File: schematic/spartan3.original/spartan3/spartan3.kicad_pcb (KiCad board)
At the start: 2 copper layers, 215.9 x 160 mm, 241 parts, among them U1_clk_select_0 SPFT_Sliding_Switch-dynacore, U2 XC3S250E-4TQG144C

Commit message: Schematics :: in/out pins mapped. PCB layout :: updated
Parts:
- removed J_CONTROL_0: Conn_01x25_Male, Connector_PinHeader_2.54mm:PinHeader_1x25_P2.54mm_Vertical
- F_pwr_0, U_pwr_vcc_banks_0, U_pwr_vcc_core_0, U_pwr_vcc_peripheral_0: moved to B.Cu
- moved X_clk_0 243.8 mm to (243.9, 44.4)
- moved U_pwr_vcc_banks_0 59.2 mm to (206.3, 50.8)
- moved U_pwr_vcc_core_0 59.1 mm to (205.7, 40.6)
- moved U_pwr_vcc_peripheral_0 59.1 mm to (205.7, 30.5)
- moved J_pwr_0 59.1 mm to (199.7, 18.1)
- moved R_eeprom_hold_0 59.1 mm to (185.4, 7.62)
- moved F_pwr_0 55.5 mm to (198.1, 22.9), turned to 180 degrees
- moved R__eeprom_dq1_0 52.8 mm to (180.3, 2.54)
- moved R_eeprom_w_0 48.0 mm to (172.7, 7.62)
- moved R_eeprom_s_0 47.4 mm to (172.7, 2.54)
- moved C_eeprom_vcc_0 39.7 mm to (180.3, 7.62)
- moved U_eeprom_0 39.4 mm to (182.9, -5.08)
- moved L_clk_0 25.0 mm to (223.5, 48.3)
- moved C_clk_1 25.0 mm to (223.5, 53.3)
- moved U2 9.51 mm to (165.1, 48.3)
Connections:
- net P63 renamed D0_DIN
- net P71 renamed CCLK
- D_out_sysbus_4 pad 2: out_sysbus_4 -> P47
- U2 pad 143: P143 -> HSWAP_EN
- U2 pad 33: P33 -> out_flags_z
- U2 pad 34: P34 -> out_flags_eq
- U2 pad 35: P35 -> out_flags_gt
- U2 pad 36: P36 -> out_flags_C_out
- U2 pad 38: P38 -> out_sysbus_0
- U2 pad 40: P40 -> out_sysbus_1
- U2 pad 41: P41 -> out_sysbus_2
- U2 pad 43: P43 -> out_sysbus_3
- U2 pad 48: P48 -> out_sysbus_5
- U2 pad 50: P50 -> out_sysbus_6
- U2 pad 51: P51 -> out_sysbus_7
- U2 pad 54: P54 -> in_manual_input_o_0
- U2 pad 57: P57 -> in_manual_input_o_1
- U2 pad 58: P58 -> in_manual_input_o_2
- U2 pad 59: P59 -> in_manual_input_o_3
- U2 pad 60: P60 -> in_manual_input_o_4
- U2 pad 62: P62 -> in_manual_input_o_5
- U2 pad 66: P66 -> in_manual_input_o_6
- U2 pad 67: P67 -> in_manual_input_o_7
- U2 pad 72: P72 -> DONE
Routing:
- net Net-(SW_pwr_0-Pad2): track 0.00 -> 336.7 mm, vias 0 -> 4
- net Net-(F_pwr_0-Pad2): track 0.00 -> 303.4 mm
- net GND: track 1549.1 -> 1824.2 mm, vias 0 -> 4
- net out_flags_C_out: track 0.00 -> 176.5 mm, vias 0 -> 1
- net out_flags_gt: track 0.00 -> 162.7 mm, vias 0 -> 1
- net out_sysbus_7: track 0.00 -> 161.8 mm, vias 0 -> 1
- net out_sysbus_6: track 0.00 -> 152.1 mm, vias 0 -> 1
- net out_flags_eq: track 0.00 -> 148.9 mm, vias 0 -> 1
- net out_sysbus_5: track 0.00 -> 141.3 mm, vias 0 -> 1
- net out_flags_z: track 0.00 -> 134.6 mm, vias 0 -> 1
- net P47: track 0.00 -> 131.5 mm, vias 0 -> 1
- net VCC_banks: track 0.00 -> 127.5 mm, vias 0 -> 9
- net out_sysbus_3: track 0.00 -> 122.3 mm, vias 0 -> 1
- net out_sysbus_2: track 0.00 -> 111.3 mm, vias 0 -> 1
- net out_sysbus_1: track 0.00 -> 101.1 mm, vias 0 -> 1
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
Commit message: Schematics :: updated. PCB layout :: updated
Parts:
- C_clk_0, C_clk_1, C_eeprom_vcc_0, L_clk_0, R_JTAG_TCK_0, R_JTAG_TDI_0, R_JTAG_TDO_0, R_JTAG_TMS_0, R__eeprom_dq1_0, R_clk_oe_0, R_clk_out_0, R_eeprom_hold_0, R_eeprom_s_0, R_eeprom_w_0, U_eeprom_0, X_clk_0: moved to B.Cu
- J_pwr_0: footprint Connector_USB:USB_A_Molex_67643_Horizontal -> Connector_USB:USB_A_Molex_105057_Vertical
- moved R_JTAG_TDI_0 108.7 mm to (182.9, 14.0), turned to 180 degrees
- moved R_clk_out_0 97.9 mm to (180.3, 54.6), turned to 180 degrees
- moved U_eeprom_0 80.2 mm to (143.4, 64.8), turned to 180 degrees
- moved R_JTAG_TCK_0 71.8 mm to (163.8, 14.0), turned to 180 degrees
- moved R__eeprom_dq1_0 68.8 mm to (151.1, 64.8), turned to 180 degrees
- moved R_eeprom_hold_0 68.5 mm to (140.9, 59.7), turned to -90 degrees
- moved R_JTAG_TDO_0 67.2 mm to (174.0, 14.0), turned to 180 degrees
- moved P_JTAG_0 65.8 mm to (160.0, 6.35)
- moved R_eeprom_w_0 63.5 mm to (151.1, 67.3), turned to 180 degrees
- moved R_eeprom_s_0 63.5 mm to (151.1, 62.2), turned to 180 degrees
- moved R_JTAG_TMS_0 62.7 mm to (153.7, 14.0), turned to 180 degrees
- moved C_eeprom_vcc_0 62.4 mm to (146.0, 59.7), turned to -90 degrees
- moved C_clk_0 54.6 mm to (206.0, 55.9)
- moved X_clk_0 47.2 mm to (200.6, 63.5)
- moved R_clk_oe_0 45.0 mm to (205.7, 63.5), turned to 180 degrees
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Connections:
- net in_manual_input_o_0 renamed P54
- net in_manual_input_o_1 renamed M2
- net in_manual_input_o_2 renamed P58
- net in_manual_input_o_3 renamed P59
- net in_manual_input_o_4 renamed M1
- net in_manual_input_o_5 renamed M0
- net in_manual_input_o_6 renamed P66
- net in_manual_input_o_7 renamed P67
- net out_flags_C_out renamed P36
- net out_flags_eq renamed P34
- net out_flags_gt renamed P35
- net out_flags_z renamed P33
- net out_sysbus_0 renamed P38
- net out_sysbus_1 renamed INIT_B
- net out_sysbus_2 renamed P41
- net out_sysbus_3 renamed DOUT_BUSY
- net out_sysbus_5 renamed P48
- net out_sysbus_6 renamed P50
- net out_sysbus_7 renamed P51
- D_in_acc_r_0 pad 1: in_acc_r -> P16
- D_in_acc_w_0 pad 1: in_acc_w -> P140
- D_in_bus1_one_0 pad 1: in_bus1 -> P4
- D_in_bus1_ps_0 pad 2: in_bus1 -> P4
- D_in_clk_manual_0 pad 1: in_clk_manual -> P94
- D_in_iar_r_0 pad 1: in_iar_r -> P18
- D_in_iar_w_0 pad 1: in_iar_w -> P142
- D_in_ir_r_0 pad 1: in_ir_r -> P17
- D_in_ir_w_0 pad 1: in_ir_w -> P141
- D_in_is_bus1_w_0 pad 1: in_is_bus1_w -> P6
- D_in_is_clk_external_0 pad 1: in_is_clk_external -> P91
- D_in_is_clk_high_0 pad 1: in_is_clk_high -> P89
- D_in_is_clk_low_0 pad 1: in_is_clk_low -> P88
- D_in_is_clk_manual_0 pad 1: in_is_clk_manual -> P87
- D_in_is_clk_veryhigh_0 pad 1: in_is_clk_veryhigh -> P92
- D_in_manual_input_r_0 pad 1: in_manual_input_r -> P7
- D_in_r0_r_0 pad 1: in_r0_r -> P14
- D_in_r0_w_0 pad 1: in_r0_w -> P122
- D_in_r1_r_0 pad 1: in_r1_r -> P12
- D_in_r1_w_0 pad 1: in_r1_w -> P120
- D_in_r2_r_0 pad 1: in_r2_r -> P10
- D_in_r2_w_0 pad 1: in_r2_w -> P119
- D_in_r3_r_0 pad 1: in_r3_r -> P8
- D_in_r3_w_0 pad 1: in_r3_w -> P117
- D_in_ram_a_w_0 pad 1: in_ram_a_w -> P139
- D_in_ram_r_0 pad 1: in_ram_r -> P15
- D_in_ram_w_0 pad 1: in_ram_w -> P136
- D_in_read_reg_en_0 pad 1: in_read_reg_en -> P20
- D_in_temp_w_0 pad 1: in_temp_w -> P123
- D_in_write_reg_en_0 pad 1: in_write_reg_en -> P2
- D_out_acc_r_0 pad 2: out_acc_r -> P132
- D_out_acc_w_0 pad 2: out_acc_w -> P96
- D_out_bus1_0 pad 2: out_bus1 -> P130
- D_out_can_read_0 pad 2: out_can_read -> P21
- D_out_can_write_0 pad 2: out_can_write -> P3
- D_out_clk_internal_0 pad 2: out_clk_internal -> P93
- D_out_clkc_0 pad 2: out_clkc -> P86
- D_out_clkr_0 pad 2: out_clkr -> P85
- D_out_clkw_0 pad 2: out_clkw -> P83
- D_out_flags_w_0 pad 2: out_flags_w -> P105
- D_out_iar_r_0 pad 2: out_iar_r -> P134
- D_out_iar_w_0 pad 2: out_iar_w -> P95
- D_out_ir_w_0 pad 2: out_ir_w -> P98
- D_out_is_bus1_w_0 pad 2: out_is_bus1_w -> P5
- D_out_r0_r_0 pad 2: out_r0_r -> P129
- D_out_r0_w_0 pad 2: out_r0_w -> P106
- D_out_r1_r_0 pad 2: out_r1_r -> P128
- D_out_r1_w_0 pad 2: out_r1_w -> P112
- D_out_r2_r_0 pad 2: out_r2_r -> P126
- D_out_r2_w_0 pad 2: out_r2_w -> P113
- D_out_r3_r_0 pad 2: out_r3_r -> P125
- D_out_r3_w_0 pad 2: out_r3_w -> P116
- D_out_ram_a_w_0 pad 2: out_ram_a_w -> P104
- D_out_ram_r_0 pad 2: out_ram_r -> P131
- D_out_ram_w_0 pad 2: out_ram_w -> P97
- D_out_s1_0 pad 2: out_s1 -> P82
- D_out_s2_0 pad 2: out_s2 -> P81
- D_out_s3_0 pad 2: out_s3 -> P77
- D_out_s4_0 pad 2: out_s4 -> P76
- D_out_s5_0 pad 2: out_s5 -> P75
- D_out_s6_0 pad 2: out_s6 -> P74
- D_out_temp_w_0 pad 2: out_temp_w -> P103
- R_in_acc_r_0 pad 1: in_acc_r -> P16
- R_in_acc_w_0 pad 1: in_acc_w -> P140
- R_in_bus1_0 pad 1: in_bus1 -> P4
- R_in_clk_manual_0 pad 1: in_clk_manual -> P94
- R_in_iar_r_0 pad 1: in_iar_r -> P18
- R_in_iar_w_0 pad 1: in_iar_w -> P142
- R_in_ir_r_0 pad 1: in_ir_r -> P17
- R_in_ir_w_0 pad 1: in_ir_w -> P141
- R_in_is_bus1_w_0 pad 1: in_is_bus1_w -> P6
- R_in_is_clk_external_0 pad 1: in_is_clk_external -> P91
- R_in_is_clk_high_0 pad 1: in_is_clk_high -> P89
- R_in_is_clk_low_0 pad 1: in_is_clk_low -> P88
- R_in_is_clk_manual_0 pad 1: in_is_clk_manual -> P87
- R_in_is_clk_veryhigh_0 pad 1: in_is_clk_veryhigh -> P92
- R_in_manual_input_r_0 pad 1: in_manual_input_r -> P7
- R_in_r0_r_0 pad 1: in_r0_r -> P14
- R_in_r0_w_0 pad 1: in_r0_w -> P122
- R_in_r1_r_0 pad 1: in_r1_r -> P12
- R_in_r1_w_0 pad 1: in_r1_w -> P120
- R_in_r2_r_0 pad 1: in_r2_r -> P10
- R_in_r2_w_0 pad 1: in_r2_w -> P119
- R_in_r3_r_0 pad 1: in_r3_r -> P8
- R_in_r3_w_0 pad 1: in_r3_w -> P117
- R_in_ram_a_w_0 pad 1: in_ram_a_w -> P139
- R_in_ram_r_0 pad 1: in_ram_r -> P15
- R_in_ram_w_0 pad 1: in_ram_w -> P136
- R_in_read_reg_en_0 pad 1: in_read_reg_en -> P20
- R_in_temp_w_0 pad 1: in_temp_w -> P123
- R_in_write_reg_en_0 pad 1: in_write_reg_en -> P2
- SW_in_acc_w_0 pad 5: in_acc_w -> P140
- SW_in_bus1_0 pad 2: in_bus1 -> P4
- SW_in_clk_manual_0 pad 1: in_clk_manual -> P94
- SW_in_iar_w_0 pad 5: in_iar_w -> P142
- SW_in_ir_w_0 pad 5: in_ir_w -> P141
- SW_in_is_bus1_w_0 pad 2: in_is_bus1_w -> P6
- SW_in_r0_w_0 pad 5: in_r0_w -> P122
- SW_in_r1_w_0 pad 5: in_r1_w -> P120
- SW_in_r2_w_0 pad 5: in_r2_w -> P119
- SW_in_r3_w_0 pad 5: in_r3_w -> P117
- SW_in_ram_a_w_0 pad 5: in_ram_a_w -> P139
- SW_in_ram_w_0 pad 5: in_ram_w -> P136
- SW_in_read_reg_en_0 pad 2: in_read_reg_en -> P20
- SW_in_temp_w_0 pad 5: in_temp_w -> P123
- SW_in_write_reg_en_0 pad 2: in_write_reg_en -> P2
- SW_read_register_0 pad 1: in_manual_input_r -> P7
- SW_read_register_0 pad 10: in_r1_r -> P12
- SW_read_register_0 pad 11: in_r2_r -> P10
- SW_read_register_0 pad 12: in_r3_r -> P8
- SW_read_register_0 pad 5: in_iar_r -> P18
- SW_read_register_0 pad 6: in_ir_r -> P17
- SW_read_register_0 pad 7: in_acc_r -> P16
- SW_read_register_0 pad 8: in_ram_r -> P15
- SW_read_register_0 pad 9: in_r0_r -> P14
- U1_clk_select_0 pad 2: in_is_clk_veryhigh -> P92
- U1_clk_select_0 pad 3: in_is_clk_external -> P91
- U1_clk_select_0 pad 4: in_is_clk_high -> P89
- U1_clk_select_0 pad 5: in_is_clk_low -> P88
- U1_clk_select_0 pad 6: in_is_clk_manual -> P87
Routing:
- net P7: track 0.00 -> 324.5 mm
- net P8: track 0.00 -> 291.7 mm
- net P10: track 0.00 -> 276.5 mm
- net P4: track 0.00 -> 273.7 mm
- net P12: track 0.00 -> 272.7 mm
- net P14: track 0.00 -> 269.1 mm
- net P5: track 0.00 -> 254.4 mm, vias 0 -> 1
- net P94: track 0.00 -> 251.8 mm
- net P15: track 0.00 -> 245.5 mm
- net P6: track 0.00 -> 233.8 mm
- net P134: track 0.00 -> 232.9 mm, vias 0 -> 1
- net P16: track 0.00 -> 223.6 mm
- net P132: track 0.00 -> 223.2 mm, vias 0 -> 1
- net P92: track 0.00 -> 221.4 mm
- net P21: track 0.00 -> 219.9 mm, vias 0 -> 1
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
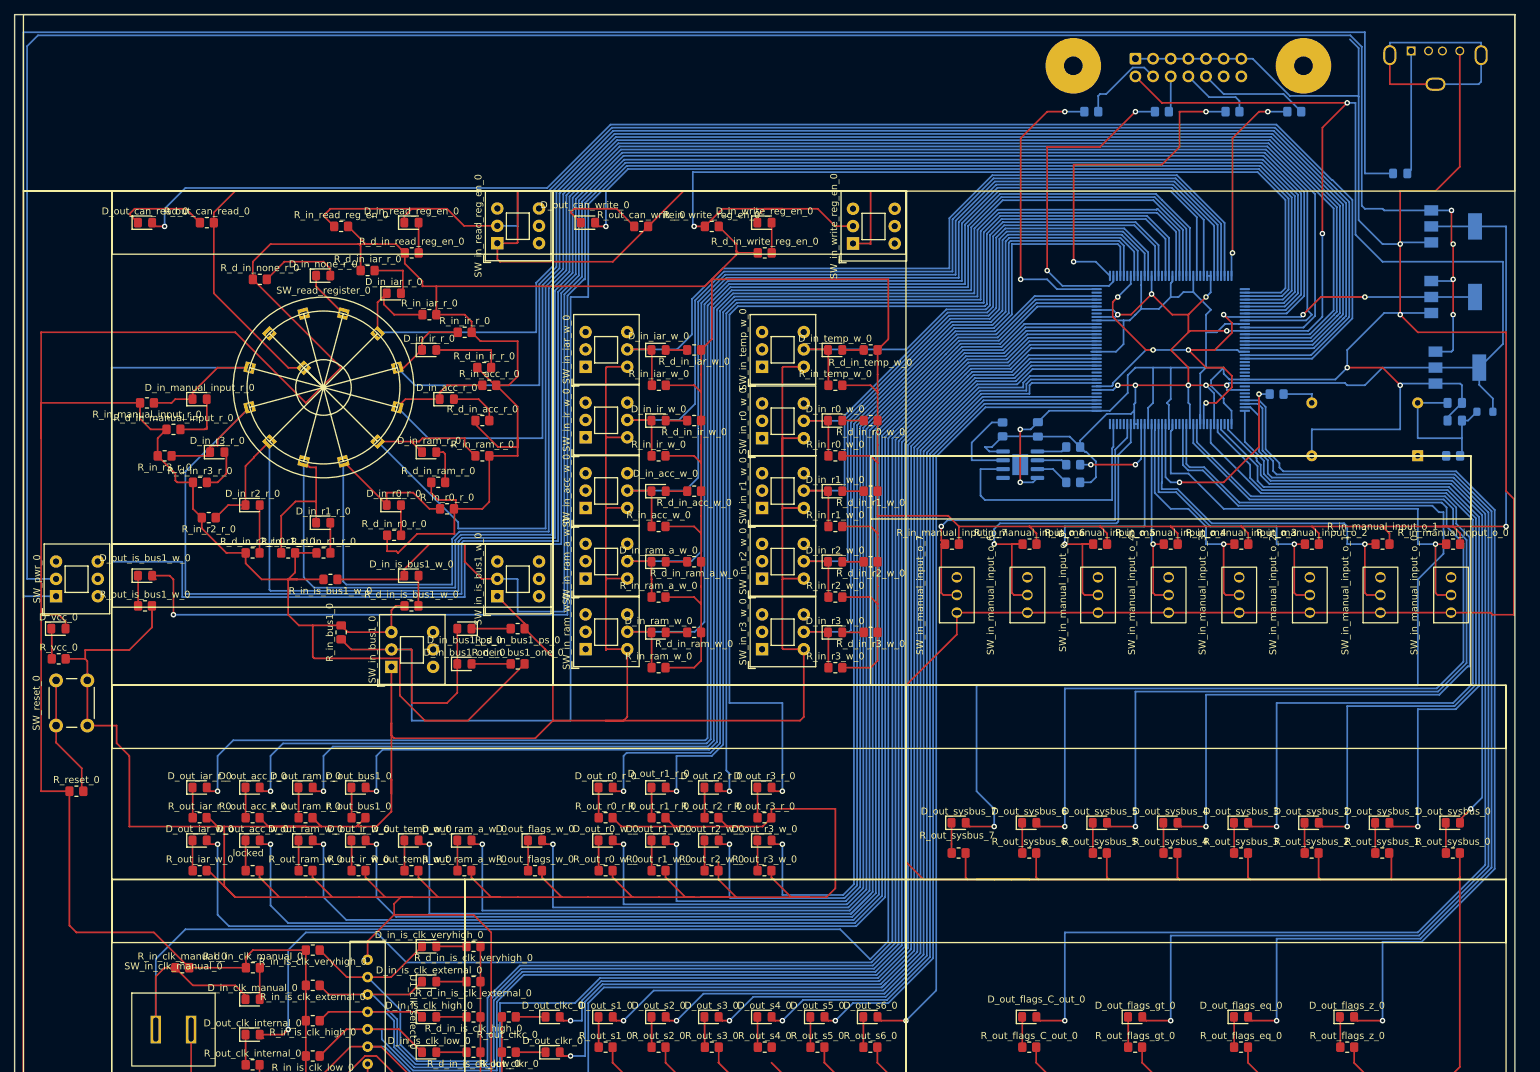
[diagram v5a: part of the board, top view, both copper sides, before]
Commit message: FPGA pins mapping added/updated. Schematics/PCB layout :: updated according to the added/updated PINs mapping
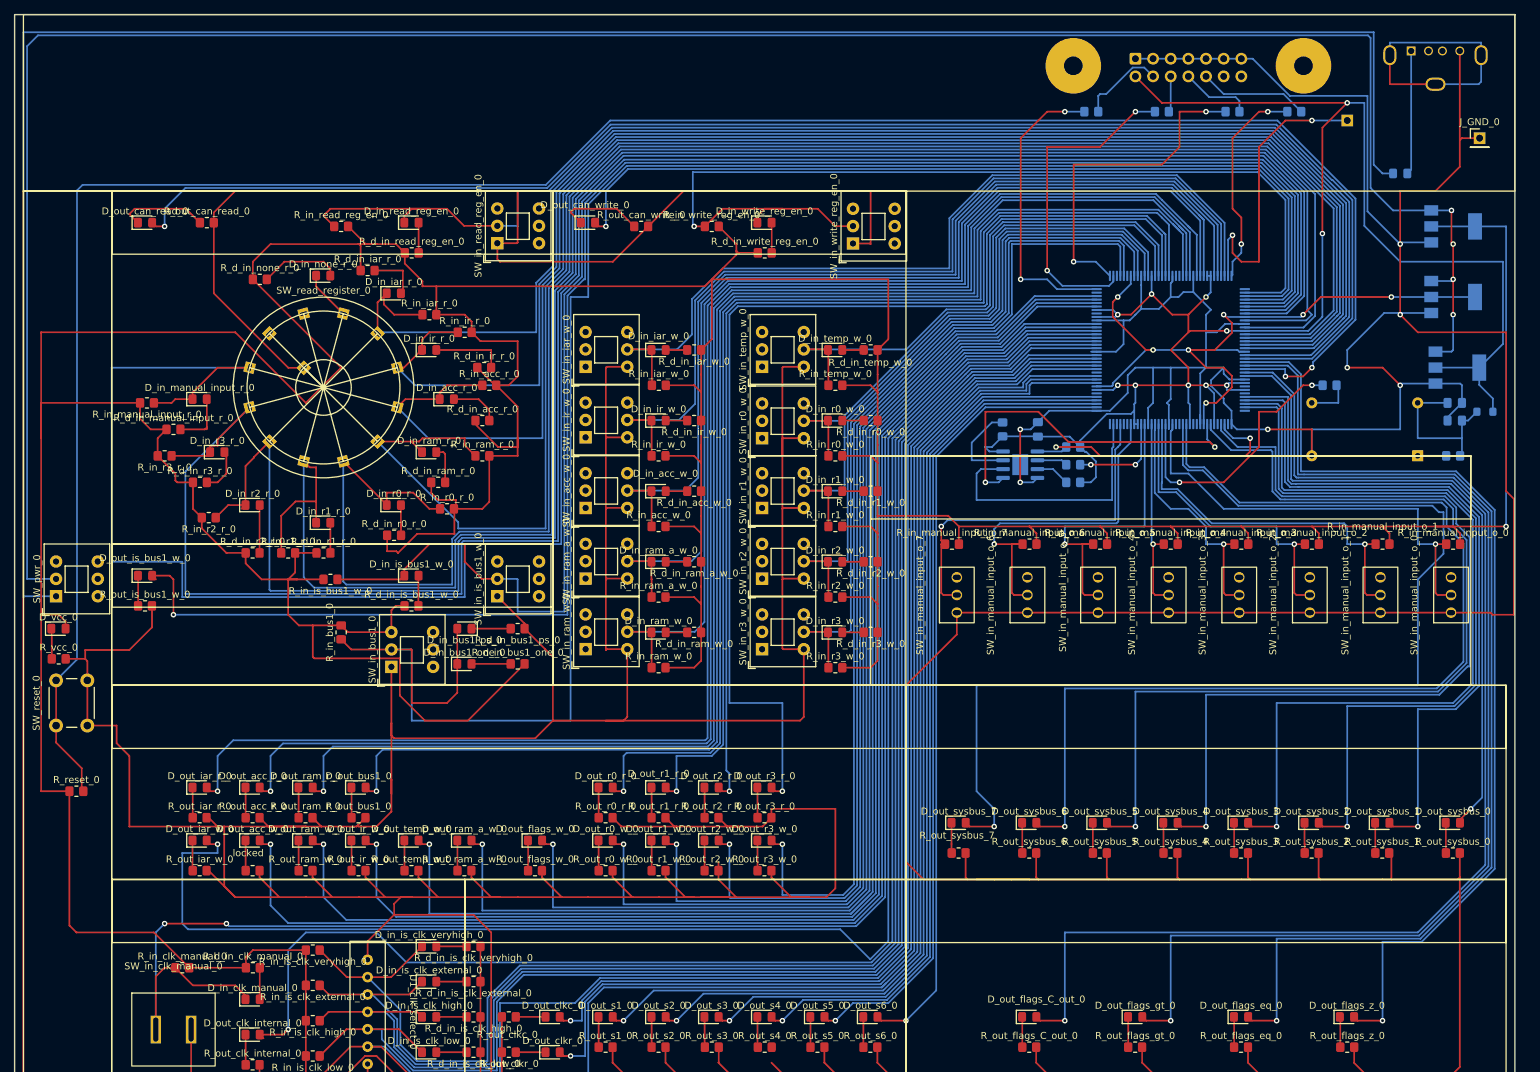
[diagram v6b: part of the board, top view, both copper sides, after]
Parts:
- added J_GND_0: Conn_01x01_Male, Connector_PinHeader_2.54mm:PinHeader_1x01_P2.54mm_Vertical, F.Cu at (209.6, 17.8)
- added J_OUT_USART1_TX_0: Conn_01x01_Male, Connector_PinHeader_2.54mm:PinHeader_1x01_P2.54mm_Vertical, B.Cu at (190.5, 15.2)
- moved R_clk_out_0 7.73 mm to (188.0, 53.3)
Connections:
- net GND renamed gnd
- D_in_clk_manual_0 pad 1: P94 -> P95
- D_out_acc_r_0 pad 2: P132 -> P134
- D_out_bus1_0 pad 2: P130 -> P131
- D_out_flags_C_out_0 pad 2: P36 -> P26
- D_out_flags_eq_0 pad 2: P34 -> P23
- D_out_flags_gt_0 pad 2: P35 -> P25
- D_out_flags_z_0 pad 2: P33 -> P22
- D_out_iar_r_0 pad 2: P134 -> P135
- D_out_iar_w_0 pad 2: P95 -> P94
- D_out_r0_r_0 pad 2: P129 -> P130
- D_out_r1_r_0 pad 2: P128 -> P126
- D_out_r2_r_0 pad 2: P126 -> P125
- D_out_r3_r_0 pad 2: P125 -> P124
- D_out_ram_r_0 pad 2: P131 -> P132
- D_out_sysbus_0 pad 2: P38 -> P32
- D_out_sysbus_1 pad 2: INIT_B -> P33
- D_out_sysbus_2 pad 2: P41 -> P34
- D_out_sysbus_3 pad 2: DOUT_BUSY -> P35
- D_out_sysbus_4 pad 2: P47 -> INIT_B
- D_out_sysbus_5 pad 2: P48 -> DOUT_BUSY
- R_eeprom_s_0 pad 2: eeprom_spi_cs_n -> P39
- R_in_clk_manual_0 pad 1: P94 -> P95
- R_in_manual_input_o_7 pad 1: P67 -> P69
- R_reset_0 pad 2: reset -> P24
- SW_in_clk_manual_0 pad 1: P94 -> P95
- SW_in_manual_input_o_7 pad 2: P67 -> P69
- SW_reset_0 pad 1: reset -> P24
- U_eeprom_0 pad 1: eeprom_spi_cs_n -> P39
- U_eeprom_0 pad 5: eeprom_spi_din -> P44
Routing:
- net P24: track 0.00 -> 320.3 mm, vias 0 -> 2
- net P135: track 0.00 -> 233.1 mm, vias 0 -> 1
- net P26: track 0.00 -> 182.0 mm, vias 0 -> 1
- net P36: track 176.6 -> 0.00 mm, vias 1 -> 0
- net P129: track 169.4 -> 0.00 mm, vias 1 -> 0
- net P25: track 0.00 -> 167.6 mm, vias 0 -> 1
- net P128: track 160.8 -> 0.04 mm, vias 1 -> 0
- net P124: track 0.00 -> 158.7 mm, vias 0 -> 1
- net P23: track 0.00 -> 155.1 mm, vias 0 -> 1
- net P22: track 0.00 -> 140.8 mm, vias 0 -> 1
- net P48: track 140.1 -> 0.00 mm, vias 1 -> 0
- net P47: track 130.4 -> 0.00 mm, vias 1 -> 0
- net P41: track 110.0 -> 0.00 mm, vias 1 -> 0
- net P32: track 0.00 -> 93.9 mm, vias 0 -> 1
- net P38: track 89.2 -> 0.00 mm, vias 1 -> 0
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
